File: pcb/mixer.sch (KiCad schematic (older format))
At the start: 43 parts

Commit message: Define pin map, clean up schematic
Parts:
- C14, C15: renamed from C?; value 100n -> 0.1u
- gave numbers to parts that had none: 41
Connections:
- net labels added: +2V5, -2V5
- net labels removed: +3V3, -3V3

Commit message: clean up ERC, more DFT stuff, started sigma delta adc
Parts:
- added R98: DNI-50, symbol Device:R
- added R99: DNI - 50, symbol Device:R
- added TP50, TP51, TP52, TP53: TestPoint, symbol Connector:TestPoint
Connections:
- wire segments 115 -> 121
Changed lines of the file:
@@
 $Descr A4 11693 8268
 encoding utf-8
-Sheet 2 6
+Sheet 2 7
 Title ""
 Date ""
@@
 Wire Wire Line
 	9300 2850 9300 2350
-Wire Wire Line
-	9650 2650 9550 2650
 $Comp
 L Device:Transformer_1P_SS T?
@@
 Wire Wire Line
 	7550 3700 7400 3700
-Wire Wire Line
-	9650 3900 9550 3900
 $Comp
 L Device:Transformer_1P_SS T?
@@
 RF_Q
 Wire Wire Line
-	5900 3850 6200 3850
+	5900 3850 6100 3850
 Wire Wire Line
 	7400 3850 7400 3700
@@
 LO_Q
 Wire Wire Line
-	5900 3400 6200 3400
+	5900 3400 6100 3400
 Wire Wire Line
 	6900 3400 6900 2450
 Wire Wire Line
-	6900 2450 7550 2450
+	6900 2450 7200 2450
 Connection ~ 5900 3400
 Text Label 6950 2450 0    50   ~ 0
@@
 $EndComp
 Wire Wire Line
-	6500 3400 6900 3400
+	6500 3400 6650 3400
 $Comp
 L Device:R R?
@@
 $EndComp
 Wire Wire Line
-	6500 3850 7400 3850
+	6500 3850 6650 3850
 $Comp
 L power:GNDA #PWR?
@@
 	-1   0    0    1
 $EndComp
+$Comp
+L Connector:TestPoint TP50
+U 1 1 60A10865
+P 6100 3400
+F 0 "TP50" H 6158 3518 50  0000 L CNN
+F 1 "TestPoint" H 6158 3427 50  0000 L CNN
+F 2 "" H 6300 3400 50  0001 C CNN
+F 3 "~" H 6300 3400 50  0001 C CNN
+	1    6100 3400
+	1    0    0    -1
+$EndComp
+Connection ~ 6100 3400
+Wire Wire Line
+	6100 3400 6200 3400
+$Comp
+L Connector:TestPoint TP52
+U 1 1 60A10D60
+P 6650 3400
+F 0 "TP52" H 6708 3518 50  0000 L CNN
+F 1 "TestPoint" H 6708 3427 50  0000 L CNN
+F 2 "" H 6850 3400 50  0001 C CNN
+F 3 "~" H 6850 3400 50  0001 C CNN
+	1    6650 3400
+	1    0    0    -1
+$EndComp
+Connection ~ 6650 3400
+Wire Wire Line
+	6650 3400 6900 3400
+$Comp
+L Connector:TestPoint TP53
+U 1 1 60A10F72
+P 6650 3850
+F 0 "TP53" H 6592 3876 50  0000 R CNN
+F 1 "TestPoint" H 6592 3967 50  0000 R CNN
+F 2 "" H 6850 3850 50  0001 C CNN
+F 3 "~" H 6850 3850 50  0001 C CNN
+	1    6650 3850
+	-1   0    0    1
+$EndComp
+Connection ~ 6650 3850
+Wire Wire Line
+	6650 3850 7100 3850
+$Comp
+L Connector:TestPoint TP51
+U 1 1 60A1186F
+P 6100 3850
+F 0 "TP51" H 6042 3876 50  0000 R CNN
+F 1 "TestPoint" H 6042 3967 50  0000 R CNN
+F 2 "" H 6300 3850 50  0001 C CNN
+F 3 "~" H 6300 3850 50  0001 C CNN
+	1    6100 3850
+	-1   0    0    1
+$EndComp
+Connection ~ 6100 3850
+Wire Wire Line
+	6100 3850 6200 3850
+$Comp
+L Device:R R?
+U 1 1 60A11B69
+P 7200 2600
+AR Path="/60A11B69" Ref="R?"  Part="1"
+AR Path="/5FB04C67/60A11B69" Ref="R99"  Part="1"
+F 0 "R99" V 6993 2600 50  0000 C CNN
+F 1 "DNI - 50" V 7084 2600 50  0000 C CNN
+F 2 "" V 7130 2600 50  0001 C CNN
+F 3 "~" H 7200 2600 50  0001 C CNN
+	1    7200 2600
+	-1   0    0    1
+$EndComp
+Connection ~ 7200 2450
+Wire Wire Line
+	7200 2450 7550 2450
+$Comp
+L Device:R R?
+U 1 1 60A12613
+P 7100 4000
+AR Path="/60A12613" Ref="R?"  Part="1"
+AR Path="/5FB04C67/60A12613" Ref="R98"  Part="1"
+F 0 "R98" V 6893 4000 50  0000 C CNN
+F 1 "DNI-50" V 6984 4000 50  0000 C CNN
+F 2 "" V 7030 4000 50  0001 C CNN
+F 3 "~" H 7100 4000 50  0001 C CNN
+	1    7100 4000
+	-1   0    0    1
+$EndComp
+Connection ~ 7100 3850
+Wire Wire Line
+	7100 3850 7400 3850
+$Comp
+L power:GNDA #PWR?
+U 1 1 60A13202
+P 7100 4150
+AR Path="/60A13202" Ref="#PWR?"  Part="1"
+AR Path="/5FB04C67/60A13202" Ref="#PWR0181"  Part="1"
+F 0 "#PWR0181" H 7100 3900 50  0001 C CNN
+F 1 "GNDA" H 7105 3977 50  0000 C CNN
+F 2 "" H 7100 4150 50  0001 C CNN
+F 3 "" H 7100 4150 50  0001 C CNN
+	1    7100 4150
+	1    0    0    -1
+$EndComp
+$Comp
+L power:GNDA #PWR?
+U 1 1 60A1375D
+P 7200 2750
+AR Path="/60A1375D" Ref="#PWR?"  Part="1"
+AR Path="/5FB04C67/60A1375D" Ref="#PWR0182"  Part="1"
+F 0 "#PWR0182" H 7200 2500 50  0001 C CNN
+F 1 "GNDA" H 7205 2577 50  0000 C CNN
+F 2 "" H 7200 2750 50  0001 C CNN
+F 3 "" H 7200 2750 50  0001 C CNN
+	1    7200 2750
+	1    0    0    -1
+$EndComp
+Wire Wire Line
+	9550 2650 9650 2650
+Wire Wire Line
+	9550 3900 9650 3900
 $EndSCHEMATC

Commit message: add ext LO connectors, more decoupling
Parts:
- added C65, C66: 10u, symbol Device:C
- added J19, J20: Conn_Coaxial, symbol Connector:Conn_Coaxial
- added JP12, JP13: SolderJumper_3_Open, symbol Jumper:SolderJumper_3_Open
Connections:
- net labels added: LO_I_EXT, LO_Q_EXT
- wire segments 121 -> 131
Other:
- moved on the sheet: R98, R99, T1, T2, T3, T4

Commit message: started assigning footprints
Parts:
- removed D1, D2, D3, D4, D5, D6, D7, D8: D_Schottky, symbol Device:D_Schottky
- added D1, D2, D3, D4: BAT15-04W, Package_TO_SOT_SMD:SOT-323_SC-70_Handsoldering, symbol Device:D_Schottky_x2_Serial_AKC
- C10, C11, C12, C13, C14, C15, C16, C17, C65, C66, C8, C9: footprint (none) -> Capacitor_SMD:C_0805_2012Metric_Pad1.15x1.40mm_HandSolder
- R10, R11, R12, R13, R14, R15, R16, R17, R18, R19, R4, R5, R6, R7, R8, R9, R98, R99: footprint (none) -> Resistor_SMD:R_0805_2012Metric_Pad1.20x1.40mm_HandSolder
- U4: footprint SOIC127P599X175-8N -> (none)
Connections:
- wire segments 131 -> 133

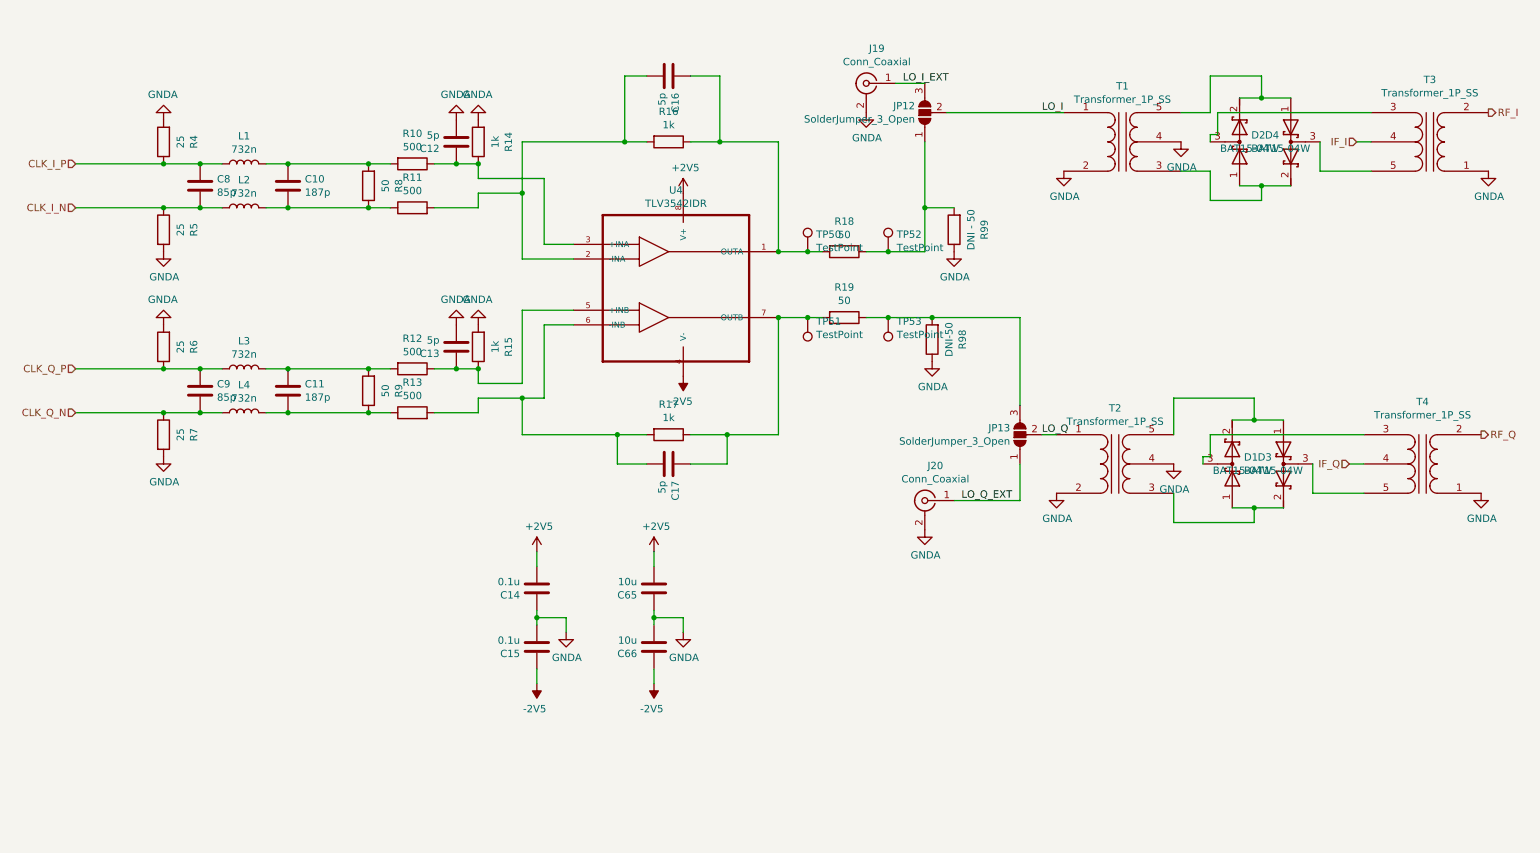
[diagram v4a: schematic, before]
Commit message: Update footprints, move to 0603 passives for JLCPCB assembly, create transformer footprints
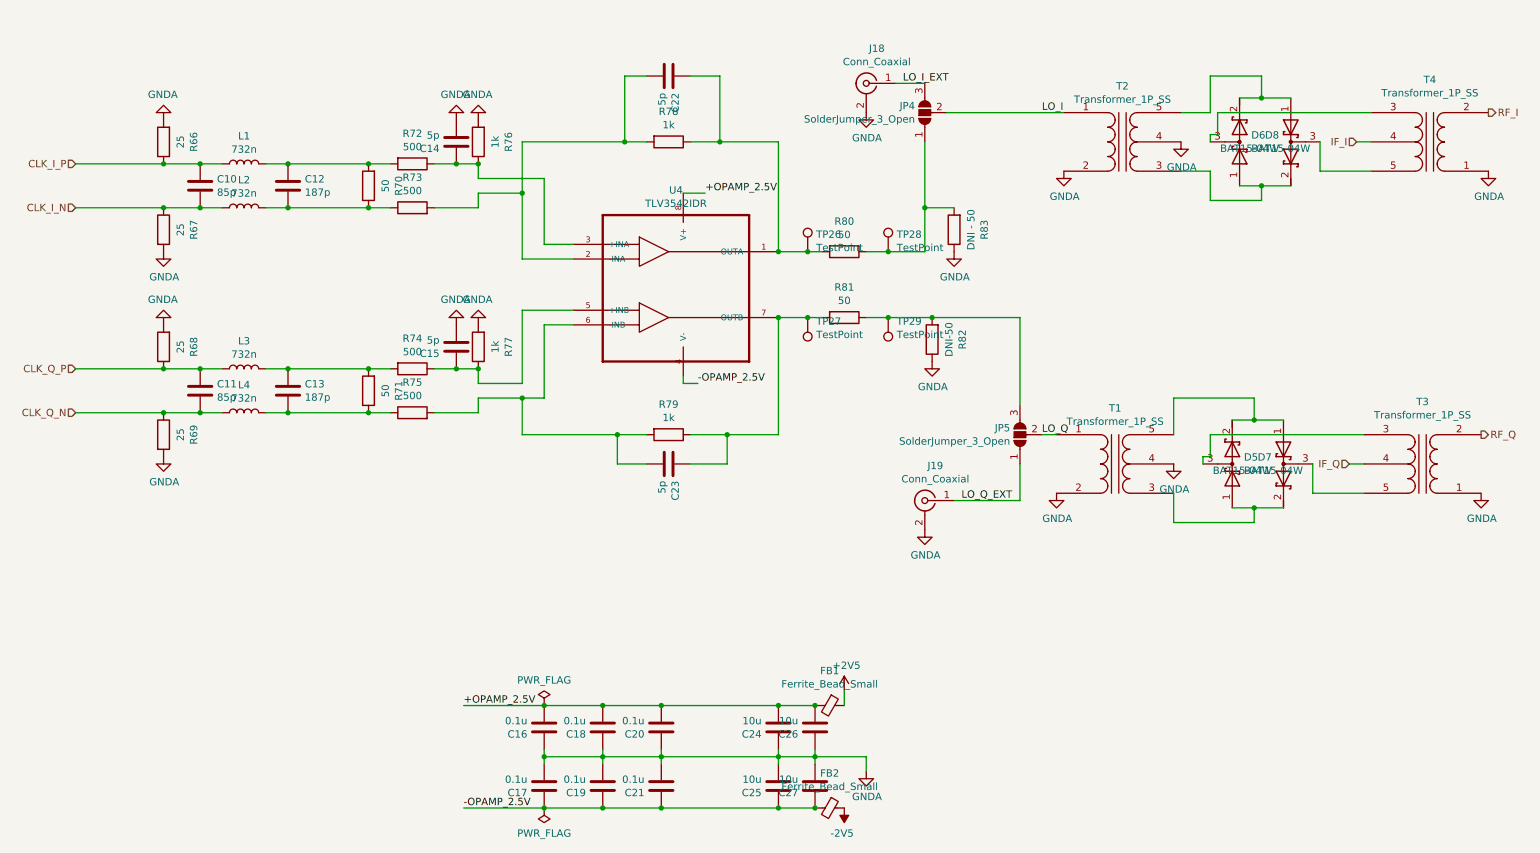
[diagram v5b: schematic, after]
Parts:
- removed C14, C15: 0.1u, Capacitor_SMD:C_0805_2012Metric_Pad1.15x1.40mm_HandSolder, symbol Device:C
- removed C65, C66: 10u, Capacitor_SMD:C_0805_2012Metric_Pad1.15x1.40mm_HandSolder, symbol Device:C
- added C16, C17, C18, C19, C20, C21: 0.1u, Capacitor_SMD:C_0603_1608Metric, symbol Device:C
- added C24, C25, C26, C27: 10u, Capacitor_SMD:C_0603_1608Metric, symbol Device:C
- added FB1, FB2: Ferrite_Bead_Small, Inductor_SMD:L_0603_1608Metric_Pad1.05x0.95mm_HandSolder, symbol Device:Ferrite_Bead_Small
- C10: renamed from C8; footprint Capacitor_SMD:C_0805_2012Metric_Pad1.15x1.40mm_HandSolder -> Capacitor_SMD:C_0603_1608Metric
- C11: renamed from C9; footprint Capacitor_SMD:C_0805_2012Metric_Pad1.15x1.40mm_HandSolder -> Capacitor_SMD:C_0603_1608Metric
- C12: renamed from C10; footprint Capacitor_SMD:C_0805_2012Metric_Pad1.15x1.40mm_HandSolder -> Capacitor_SMD:C_0603_1608Metric
- C13: renamed from C11; footprint Capacitor_SMD:C_0805_2012Metric_Pad1.15x1.40mm_HandSolder -> Capacitor_SMD:C_0603_1608Metric
- C14: renamed from C12; footprint Capacitor_SMD:C_0805_2012Metric_Pad1.15x1.40mm_HandSolder -> Capacitor_SMD:C_0603_1608Metric
- C15: renamed from C13; footprint Capacitor_SMD:C_0805_2012Metric_Pad1.15x1.40mm_HandSolder -> Capacitor_SMD:C_0603_1608Metric
- C22: renamed from C16; footprint Capacitor_SMD:C_0805_2012Metric_Pad1.15x1.40mm_HandSolder -> Capacitor_SMD:C_0603_1608Metric
- C23: renamed from C17; footprint Capacitor_SMD:C_0805_2012Metric_Pad1.15x1.40mm_HandSolder -> Capacitor_SMD:C_0603_1608Metric
- J18: renamed from J19; footprint (none) -> Connector_Coaxial:SMA_Amphenol_132289_EdgeMount
- J19: renamed from J20; footprint (none) -> Connector_Coaxial:SMA_Amphenol_132289_EdgeMount
- L1, L2, L3, L4: footprint (none) -> Inductor_SMD:L_0603_1608Metric_Pad1.05x0.95mm_HandSolder
- R66: renamed from R4; footprint Resistor_SMD:R_0805_2012Metric_Pad1.20x1.40mm_HandSolder -> Resistor_SMD:R_0603_1608Metric
- R67: renamed from R5; footprint Resistor_SMD:R_0805_2012Metric_Pad1.20x1.40mm_HandSolder -> Resistor_SMD:R_0603_1608Metric
- R68: renamed from R6; footprint Resistor_SMD:R_0805_2012Metric_Pad1.20x1.40mm_HandSolder -> Resistor_SMD:R_0603_1608Metric
- R69: renamed from R7; footprint Resistor_SMD:R_0805_2012Metric_Pad1.20x1.40mm_HandSolder -> Resistor_SMD:R_0603_1608Metric
- R70: renamed from R8; footprint Resistor_SMD:R_0805_2012Metric_Pad1.20x1.40mm_HandSolder -> Resistor_SMD:R_0603_1608Metric
- R71: renamed from R9; footprint Resistor_SMD:R_0805_2012Metric_Pad1.20x1.40mm_HandSolder -> Resistor_SMD:R_0603_1608Metric
- R72: renamed from R10; footprint Resistor_SMD:R_0805_2012Metric_Pad1.20x1.40mm_HandSolder -> Resistor_SMD:R_0603_1608Metric
- R73: renamed from R11; footprint Resistor_SMD:R_0805_2012Metric_Pad1.20x1.40mm_HandSolder -> Resistor_SMD:R_0603_1608Metric
- R74: renamed from R12; footprint Resistor_SMD:R_0805_2012Metric_Pad1.20x1.40mm_HandSolder -> Resistor_SMD:R_0603_1608Metric
- R75: renamed from R13; footprint Resistor_SMD:R_0805_2012Metric_Pad1.20x1.40mm_HandSolder -> Resistor_SMD:R_0603_1608Metric
- R76: renamed from R14; footprint Resistor_SMD:R_0805_2012Metric_Pad1.20x1.40mm_HandSolder -> Resistor_SMD:R_0603_1608Metric
- R77: renamed from R15; footprint Resistor_SMD:R_0805_2012Metric_Pad1.20x1.40mm_HandSolder -> Resistor_SMD:R_0603_1608Metric
- R78: renamed from R16; footprint Resistor_SMD:R_0805_2012Metric_Pad1.20x1.40mm_HandSolder -> Resistor_SMD:R_0603_1608Metric
- R79: renamed from R17; footprint Resistor_SMD:R_0805_2012Metric_Pad1.20x1.40mm_HandSolder -> Resistor_SMD:R_0603_1608Metric
- R80: renamed from R18; footprint Resistor_SMD:R_0805_2012Metric_Pad1.20x1.40mm_HandSolder -> Resistor_SMD:R_0603_1608Metric
- R81: renamed from R19; footprint Resistor_SMD:R_0805_2012Metric_Pad1.20x1.40mm_HandSolder -> Resistor_SMD:R_0603_1608Metric
- R82: renamed from R98; footprint Resistor_SMD:R_0805_2012Metric_Pad1.20x1.40mm_HandSolder -> Resistor_SMD:R_0603_1608Metric
- R83: renamed from R99; footprint Resistor_SMD:R_0805_2012Metric_Pad1.20x1.40mm_HandSolder -> Resistor_SMD:R_0603_1608Metric
- T1: renamed from T2; footprint (none) -> iq_siggen:trifilar_wound_toroidal_rf_transformer
- T2: renamed from T1; footprint (none) -> iq_siggen:trifilar_wound_toroidal_rf_transformer
- T3: renamed from T4; footprint (none) -> iq_siggen:trifilar_wound_toroidal_rf_transformer
- T4: renamed from T3; footprint (none) -> iq_siggen:trifilar_wound_toroidal_rf_transformer
- TP26: renamed from TP50; footprint (none) -> TestPoint:TestPoint_Pad_D1.5mm
- TP27: renamed from TP51; footprint (none) -> TestPoint:TestPoint_Pad_D1.5mm
- TP28: renamed from TP52; footprint (none) -> TestPoint:TestPoint_Pad_D1.5mm
- TP29: renamed from TP53; footprint (none) -> TestPoint:TestPoint_Pad_D1.5mm
- U4: footprint (none) -> Package_SO:SOIC-8_3.9x4.9mm_P1.27mm
- renumbered D1 to D5, D2 to D6, D3 to D7, D4 to D8, JP12 to JP4, JP13 to JP5
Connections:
- net +2V5: now also FB1.1; no longer U4.8 (V+)
- net -2V5: now also FB2.1; no longer U4.4 (V-)
- net GNDA: now also C16.1, C17.2, C18.1, C19.2, C20.1, C21.2, C24.1, C25.2, C26.1, C27.2
- new net +OPAMP_2.5V: C16.2, C18.2, C20.2, C24.2, C26.2, FB1.2, U4.8 (V+)
- new net -OPAMP_2.5V: C17.1, C19.1, C21.1, C25.1, C27.1, FB2.2, U4.4 (V-)

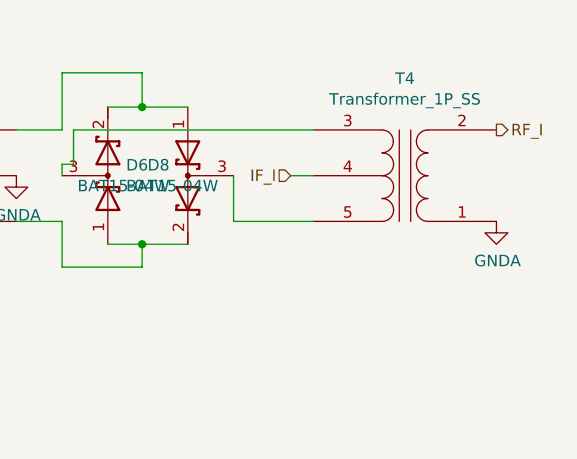
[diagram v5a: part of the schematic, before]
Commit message: routing mixer
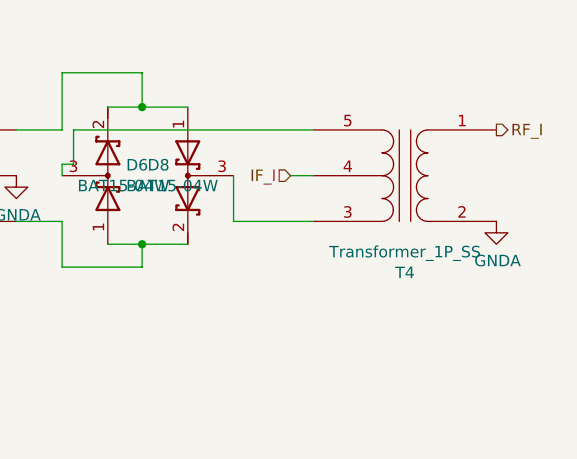
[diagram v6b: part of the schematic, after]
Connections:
- net GNDA: now also T4.2 (AB); no longer T4.1 (AA)
- net RF_I: now also T4.1 (AA); no longer T4.2 (AB)
- net at T4.3 (SA): now also D8.3 (common); no longer D6.3 (common)
- net at T4.5 (SB): now also D6.3 (common); no longer D8.3 (common)
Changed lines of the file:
@@
 F 3 "~" H 10350 2650 50  0001 C CNN
 	1    10350 2650
-	-1   0    0    1
+	-1   0    0    -1
 $EndComp
 Wire Wire Line

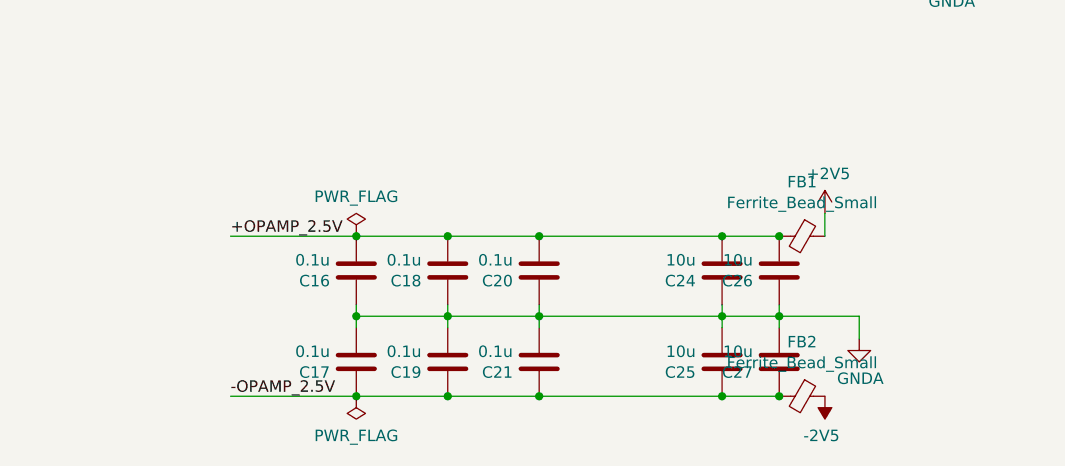
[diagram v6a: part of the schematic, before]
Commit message: lined up data bus resistors, done 5v reg, started the -5V switching regulator
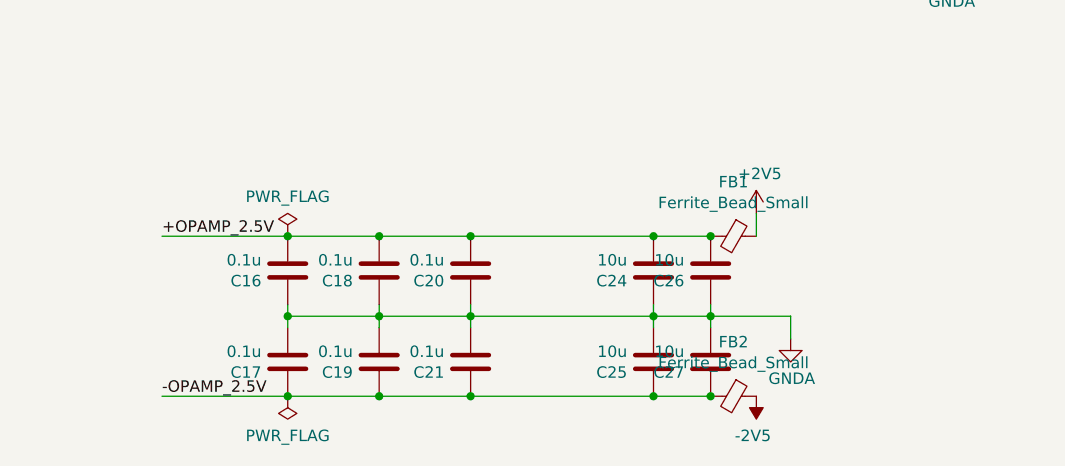
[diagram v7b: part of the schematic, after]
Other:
- moved on the sheet: C16, C17, C18, C19, C20, C21, C24, C25, C26, C27, FB1, FB2

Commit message: finish up vregs, routed filters, iq baseband outputs
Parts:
- FB1, FB2: footprint Inductor_SMD:L_0603_1608Metric_Pad1.05x0.95mm_HandSolder -> Inductor_SMD:L_0805_2012Metric_Pad1.05x1.20mm_HandSolder
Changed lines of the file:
@@
 F 0 "FB1" V 5713 6500 50  0000 C CNN
 F 1 "Ferrite_Bead_Small" V 5804 6500 50  0000 C CNN
-F 2 "Inductor_SMD:L_0603_1608Metric_Pad1.05x0.95mm_HandSolder" V 5880 6500 50  0001 C CNN
+F 2 "Inductor_SMD:L_0805_2012Metric_Pad1.05x1.20mm_HandSolder" V 5880 6500 50  0001 C CNN
 F 3 "~" H 5950 6500 50  0001 C CNN
 	1    5950 6500
@@
 F 0 "FB2" V 5713 7200 50  0000 C CNN
 F 1 "Ferrite_Bead_Small" V 5804 7200 50  0000 C CNN
-F 2 "Inductor_SMD:L_0603_1608Metric_Pad1.05x0.95mm_HandSolder" V 5880 7200 50  0001 C CNN
+F 2 "Inductor_SMD:L_0805_2012Metric_Pad1.05x1.20mm_HandSolder" V 5880 7200 50  0001 C CNN
 F 3 "~" H 5950 7200 50  0001 C CNN
 	1    5950 7200
